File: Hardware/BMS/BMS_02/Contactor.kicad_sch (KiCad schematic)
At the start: 34 parts, among them Q1 Q_NMOS_GSD, Q35 Q_PMOS_GDS, Q58 RQ3G100GNTB, Q59 RQ3G100GNTB, U15 TLX9185A(GBTPL,F, U16 TLX9185A(GBTPL,F

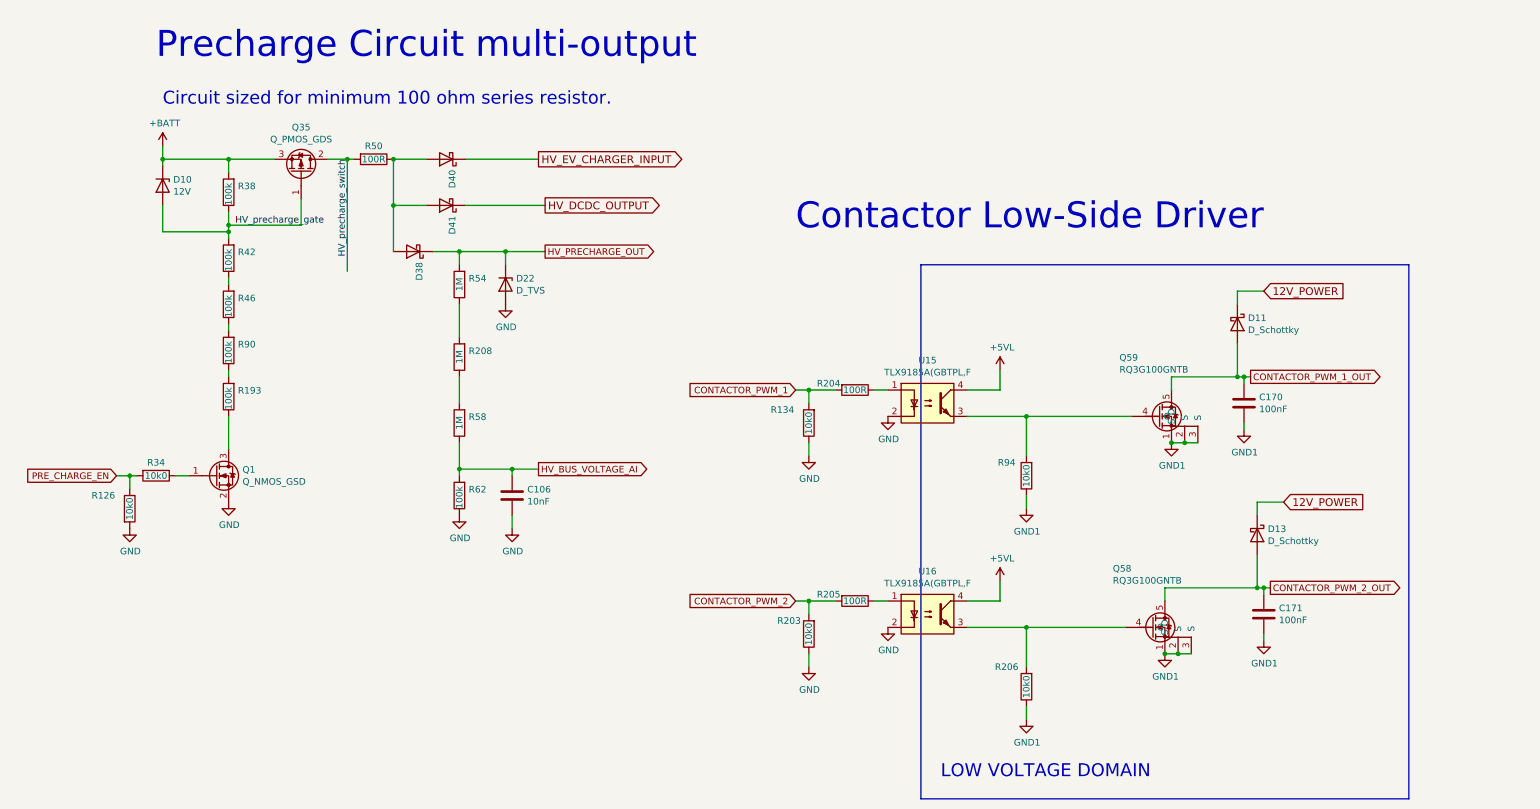
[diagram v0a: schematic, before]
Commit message: bms 02 build and code bring up. Board is built, bootloader is stable and uploads app flawlessly.
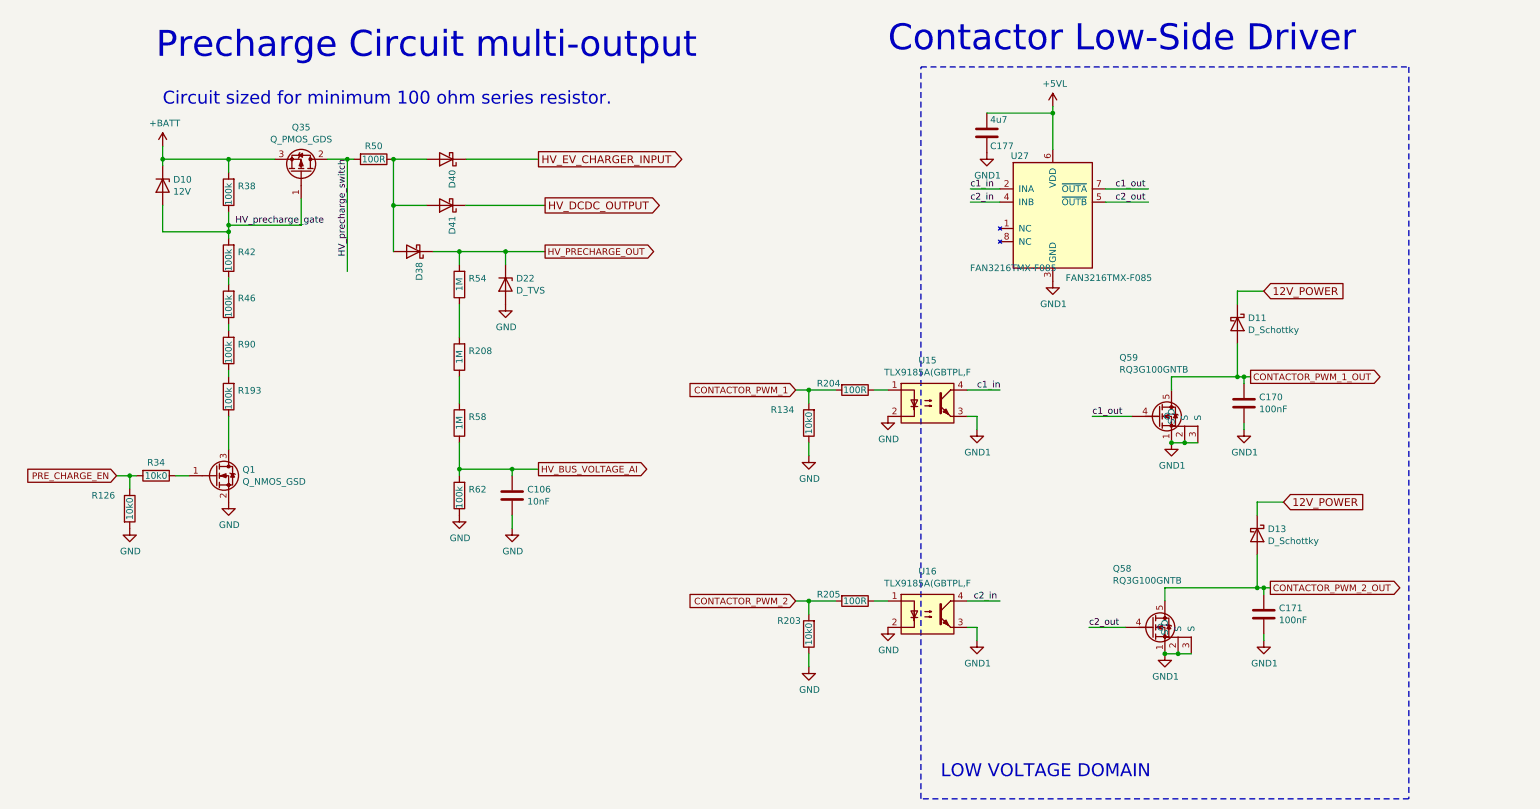
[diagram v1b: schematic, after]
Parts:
- removed R206, R94: 10k0, Resistor_SMD:R_0603_1608Metric, symbol Device:R
- added C177: 4u7, Capacitor_SMD:C_1206_3216Metric, symbol Device:C
- added U27: FAN3216TMX-F085, Package_SO:SOIC-8_3.9x4.9mm_P1.27mm, symbol ICs:FAN3216TMX-F085
- R208, R54, R58: DNP < ... > -> (none)
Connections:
- net +5VL: now also C177.2, U27.6 (VDD); no longer U15.4, U16.4
- net GND1: now also U15.3, U16.3, C177.1, U27.3 (GND)
- net c1_out: now reaches Q59.4 (G)
- net c1_out: now also U27.7 (~{OUTA}); no longer U15.3
- net c2_out: now reaches Q58.4 (G)
- net c2_out: now also U27.5 (~{OUTB}); no longer U16.3
- new net c1_in: U15.4, U27.2 (INA)
- new net c2_in: U16.4, U27.4 (INB)
